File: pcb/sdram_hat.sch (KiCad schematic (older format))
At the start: 29 parts, among them J1 CONN_02X20, J2 CONN_02X20, J3 CONN_02X20, J4 CONN_02X20, J5 AUDIO_OUT_JACK

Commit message: Add a bunch of decoupling caps to PCB
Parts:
- added C14, C15, C16, C17, C?: 100nF, Capacitors_SMD:C_0805_HandSoldering, symbol C_Small
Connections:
- wire segments 429 -> 439
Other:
- moved on the sheet: R7
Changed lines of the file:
@@
 Text GLabel 12450 3800 2    49   Input ~ 0
 DAC_SFOR0
-Text GLabel 10700 3900 2    49   Input ~ 0
+Text GLabel 10700 4000 2    49   Input ~ 0
 DAC_SFOR1
 Text GLabel 12450 3700 2    49   Input ~ 0
@@
 L GNDA #PWR051
 U 1 1 59A5B04F
-P 1700 9450
-F 0 "#PWR051" H 1700 9200 50  0001 C CNN
-F 1 "GNDA" H 1700 9300 50  0000 C CNN
-F 2 "" H 1700 9450 50  0001 C CNN
-F 3 "" H 1700 9450 50  0001 C CNN
-	1    1700 9450
+P 1700 9750
+F 0 "#PWR051" H 1700 9500 50  0001 C CNN
+F 1 "GNDA" H 1700 9600 50  0000 C CNN
+F 2 "" H 1700 9750 50  0001 C CNN
+F 3 "" H 1700 9750 50  0001 C CNN
+	1    1700 9750
 	1    0    0    -1
 $EndComp
@@
 L GND #PWR052
 U 1 1 59A5B0A5
-P 2200 9450
-F 0 "#PWR052" H 2200 9200 50  0001 C CNN
-F 1 "GND" H 2200 9300 50  0000 C CNN
-F 2 "" H 2200 9450 50  0001 C CNN
-F 3 "" H 2200 9450 50  0001 C CNN
-	1    2200 9450
-	1    0    0    -1
-$EndComp
-Wire Wire Line
-	2050 9350 2200 9350
-Wire Wire Line
-	2200 9350 2200 9450
-Wire Wire Line
-	1700 9350 1750 9350
-Wire Wire Line
-	1700 9350 1700 9450
+P 2200 9750
+F 0 "#PWR052" H 2200 9500 50  0001 C CNN
+F 1 "GND" H 2200 9600 50  0000 C CNN
+F 2 "" H 2200 9750 50  0001 C CNN
+F 3 "" H 2200 9750 50  0001 C CNN
+	1    2200 9750
+	1    0    0    -1
+$EndComp
+Wire Wire Line
+	2050 9650 2200 9650
+Wire Wire Line
+	2200 9650 2200 9750
+Wire Wire Line
+	1700 9650 1750 9650
+Wire Wire Line
+	1700 9650 1700 9750
 $Comp
 L GNDA #PWR053
@@
 L GND #PWR058
 U 1 1 59A35402
-P 2250 4200
-F 0 "#PWR058" H 2250 3950 50  0001 C CNN
-F 1 "GND" H 2250 4050 50  0000 C CNN
-F 2 "" H 2250 4200 50  0001 C CNN
-F 3 "" H 2250 4200 50  0001 C CNN
-	1    2250 4200
+P 2250 3350
+F 0 "#PWR058" H 2250 3100 50  0001 C CNN
+F 1 "GND" H 2250 3200 50  0000 C CNN
+F 2 "" H 2250 3350 50  0001 C CNN
+F 3 "" H 2250 3350 50  0001 C CNN
+	1    2250 3350
 	-1   0    0    1
 $EndComp
@@
 Connection ~ 2150 4650
 Wire Wire Line
-	1750 4200 1750 4750
+	1750 3350 1750 4750
 Wire Wire Line
 	1750 4650 1950 4650
@@
 	2100 4400 2250 4400
 Wire Wire Line
-	2250 4200 2250 4750
+	2250 3350 2250 4750
 Wire Wire Line
 	1750 4400 1900 4400
@@
 L +3.3V #PWR059
 U 1 1 599FF45F
-P 1750 4200
-F 0 "#PWR059" H 1750 4050 50  0001 C CNN
-F 1 "+3.3V" H 1750 4340 50  0000 C CNN
-F 2 "" H 1750 4200 50  0001 C CNN
-F 3 "" H 1750 4200 50  0001 C CNN
-	1    1750 4200
+P 1750 3350
+F 0 "#PWR059" H 1750 3200 50  0001 C CNN
+F 1 "+3.3V" H 1750 3490 50  0000 C CNN
+F 2 "" H 1750 3350 50  0001 C CNN
+F 3 "" H 1750 3350 50  0001 C CNN
+	1    1750 3350
 	1    0    0    -1
 $EndComp
@@
 L GND #PWR060
 U 1 1 59A39FAB
-P 2250 7900
-F 0 "#PWR060" H 2250 7650 50  0001 C CNN
-F 1 "GND" H 2250 7750 50  0000 C CNN
-F 2 "" H 2250 7900 50  0001 C CNN
-F 3 "" H 2250 7900 50  0001 C CNN
-	1    2250 7900
+P 2250 8950
+F 0 "#PWR060" H 2250 8700 50  0001 C CNN
+F 1 "GND" H 2250 8800 50  0000 C CNN
+F 2 "" H 2250 8950 50  0001 C CNN
+F 3 "" H 2250 8950 50  0001 C CNN
+	1    2250 8950
 	-1   0    0    -1
 $EndComp
@@
 	2000 7700 2250 7700
 Wire Wire Line
-	2250 7900 2250 7350
+	2250 7350 2250 8950
 Connection ~ 1550 7700
 $Comp
 L +3.3V #PWR061
 U 1 1 59A39FBB
-P 1550 7900
-F 0 "#PWR061" H 1550 7750 50  0001 C CNN
-F 1 "+3.3V" H 1550 8040 50  0000 C CNN
-F 2 "" H 1550 7900 50  0001 C CNN
-F 3 "" H 1550 7900 50  0001 C CNN
-	1    1550 7900
+P 1550 8950
+F 0 "#PWR061" H 1550 8800 50  0001 C CNN
+F 1 "+3.3V" H 1550 9090 50  0000 C CNN
+F 2 "" H 1550 8950 50  0001 C CNN
+F 3 "" H 1550 8950 50  0001 C CNN
+	1    1550 8950
 	1    0    0    1
 $EndComp
@@
 	1550 7700 1800 7700
 Wire Wire Line
-	1550 7350 1550 7900
+	1550 7350 1550 8950
 Wire Wire Line
 	4700 6450 4750 6450
@@
 L R R7
 U 1 1 59A3F1BA
-P 1900 9350
-F 0 "R7" V 1980 9350 50  0000 C CNN
-F 1 "0" V 1900 9350 50  0000 C CNN
-F 2 "Resistors_SMD:R_0805_HandSoldering" V 1830 9350 50  0001 C CNN
-F 3 "" H 1900 9350 50  0001 C CNN
-	1    1900 9350
+P 1900 9650
+F 0 "R7" V 1980 9650 50  0000 C CNN
+F 1 "0" V 1900 9650 50  0000 C CNN
+F 2 "Resistors_SMD:R_0805_HandSoldering" V 1830 9650 50  0001 C CNN
+F 3 "" H 1900 9650 50  0001 C CNN
+	1    1900 9650
 	0    1    1    0
 $EndComp
+$Comp
+L C_Small C17
+U 1 1 59A3DB18
+P 2000 4000
+F 0 "C17" H 2010 4070 50  0000 L CNN
+F 1 "100nF" H 2010 3920 50  0000 L CNN
+F 2 "Capacitors_SMD:C_0805_HandSoldering" H 2000 4000 50  0001 C CNN
+F 3 "" H 2000 4000 50  0001 C CNN
+	1    2000 4000
+	0    1    -1   0
+$EndComp
+Wire Wire Line
+	2100 4000 2250 4000
+Connection ~ 2250 4000
+Wire Wire Line
+	1900 4000 1750 4000
+Connection ~ 1750 4000
+$Comp
+L C_Small C16
+U 1 1 59A3F0C5
+P 2000 3550
+F 0 "C16" H 2010 3620 50  0000 L CNN
+F 1 "100nF" H 2010 3470 50  0000 L CNN
+F 2 "Capacitors_SMD:C_0805_HandSoldering" H 2000 3550 50  0001 C CNN
+F 3 "" H 2000 3550 50  0001 C CNN
+	1    2000 3550
+	0    1    -1   0
+$EndComp
+Wire Wire Line
+	1900 3550 1750 3550
+Connection ~ 1750 3550
+Wire Wire Line
+	2100 3550 2250 3550
+Connection ~ 2250 3550
+$Comp
+L C_Small C14
+U 1 1 59A404D1
+P 1900 8050
+F 0 "C14" H 1910 8120 50  0000 L CNN
+F 1 "100nF" H 1910 7970 50  0000 L CNN
+F 2 "Capacitors_SMD:C_0805_HandSoldering" H 1900 8050 50  0001 C CNN
+F 3 "" H 1900 8050 50  0001 C CNN
+	1    1900 8050
+	0    1    1    0
+$EndComp
+$Comp
+L C_Small C15
+U 1 1 59A4054B
+P 1900 8400
+F 0 "C15" H 1910 8470 50  0000 L CNN
+F 1 "100nF" H 1910 8320 50  0000 L CNN
+F 2 "Capacitors_SMD:C_0805_HandSoldering" H 1900 8400 50  0001 C CNN
+F 3 "" H 1900 8400 50  0001 C CNN
+	1    1900 8400
+	0    1    1    0
+$EndComp
+Wire Wire Line
+	1800 8400 1550 8400
+Connection ~ 1550 8400
+Wire Wire Line
+	1800 8050 1550 8050
+Connection ~ 1550 8050
+Wire Wire Line
+	2000 8050 2250 8050
+Connection ~ 2250 8050
+Wire Wire Line
+	2000 8400 2250 8400
+Connection ~ 2250 8400
+$Comp
+L C_Small C?
+U 1 1 59A41C71
+P 1900 8800
+F 0 "C?" H 1910 8870 50  0000 L CNN
+F 1 "100nF" H 1910 8720 50  0000 L CNN
+F 2 "Capacitors_SMD:C_0805_HandSoldering" H 1900 8800 50  0001 C CNN
+F 3 "" H 1900 8800 50  0001 C CNN
+	1    1900 8800
+	0    1    1    0
+$EndComp
+Wire Wire Line
+	2000 8800 2250 8800
+Connection ~ 2250 8800
+Wire Wire Line
+	1550 8800 1800 8800
+Connection ~ 1550 8800
 $EndSCHEMATC

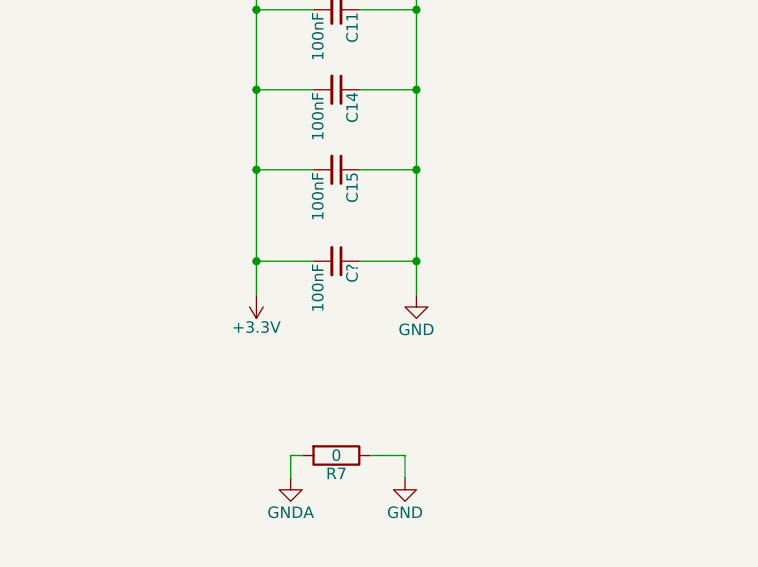
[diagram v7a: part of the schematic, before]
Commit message: Fix footprint size for SOIC package QPI flash
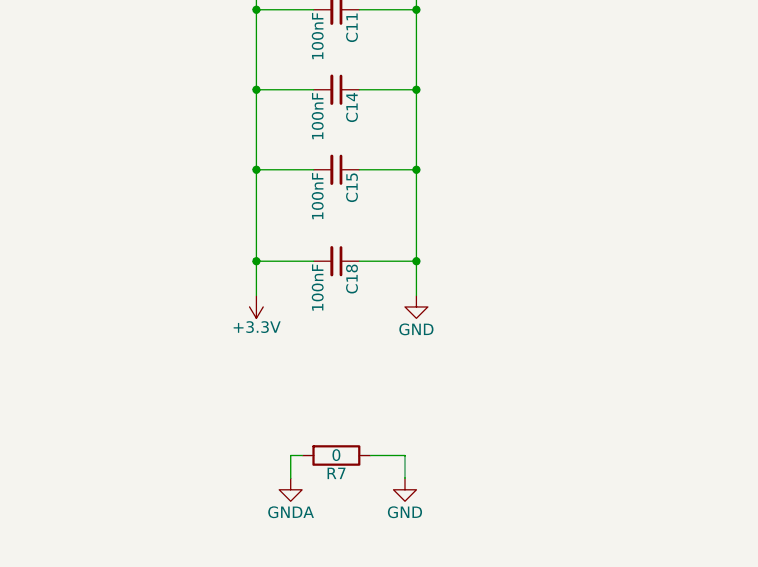
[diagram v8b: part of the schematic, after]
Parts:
- QPI_FLASH1: footprint pcb:SOIC-16_3.9x9.9mm_Pitch1.27mm_ExtendedPad -> pcb:SOIC-16_7.5x9.9mm_Pitch1.27mm_ExtendedPad
- gave numbers to parts that had none: 1
